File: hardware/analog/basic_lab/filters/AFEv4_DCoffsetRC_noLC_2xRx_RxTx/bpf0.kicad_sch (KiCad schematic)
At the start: 8 parts

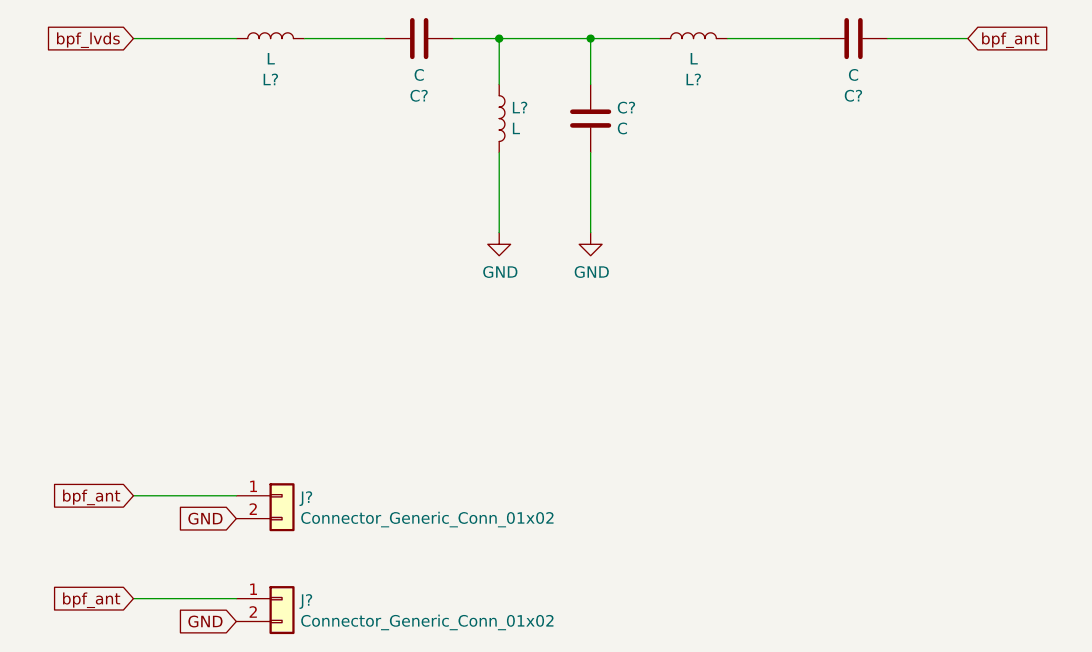
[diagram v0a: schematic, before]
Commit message: started 2xRx / RxTx PCBs with no / simple LC filters
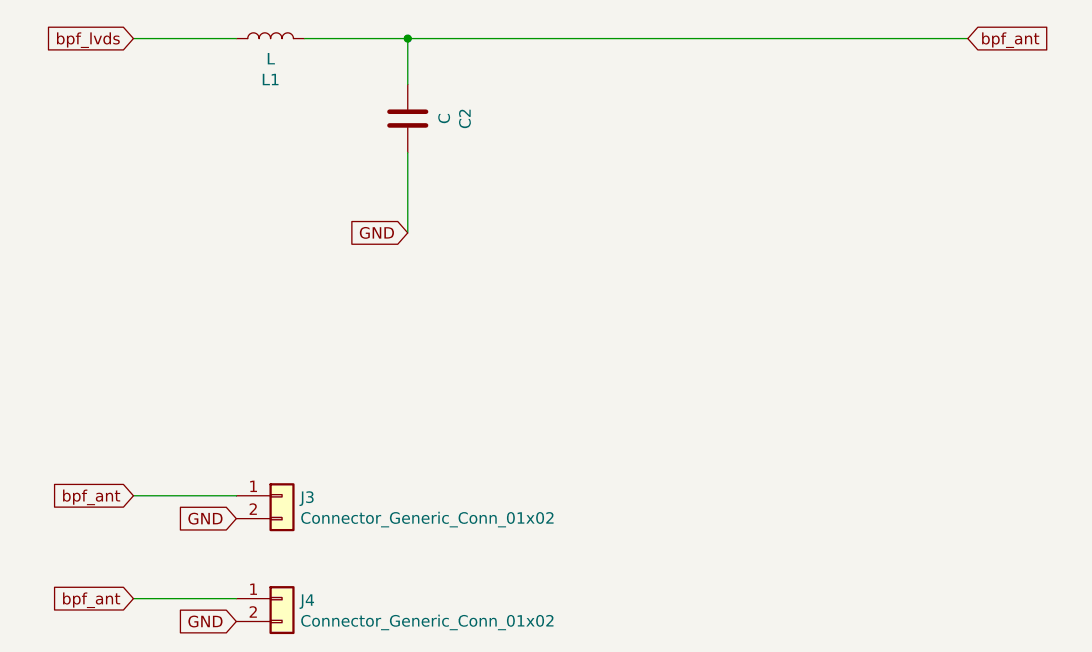
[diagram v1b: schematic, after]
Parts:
- removed C? (x2): C, Capacitor_THT:C_Axial_L3.8mm_D2.6mm_P7.50mm_Horizontal, symbol Device:C
- removed L? (x2): L, Inductor_THT:L_Toroid_Horizontal_D12.7mm_P20.00mm_Diameter14-5mm_Amidon-T50, symbol Device:L
- gave numbers to parts that had none: 4
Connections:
- net GND: now also C2.1
- net bpf_ant: now also C2.2, L1.2
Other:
- moved on the sheet: C2
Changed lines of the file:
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@@
 (kicad_sch (version 20211123) (generator eeschema)
   (paper "A4")
-  (junction (at 105.41 68.58) (diameter 0) (color 0 0 0 0)
-  )
-  (junction (at 95.25 68.58) (diameter 0) (color 0 0 0 0)
-  )
-  (wire (pts (xy 95.25 73.66) (xy 95.25 68.58))
-    (stroke (width 0) (type default) (color 0 0 0 0))
+  (junction (at 85.09 68.58) (diameter 0) (color 0 0 0 0)
   )
   (wire (pts (xy 54.61 119.38) (xy 66.04 119.38))
     (stroke (width 0) (type default) (color 0 0 0 0))
   )
-  (wire (pts (xy 95.25 68.58) (xy 90.17 68.58))
+  (wire (pts (xy 85.09 68.58) (xy 85.09 73.66))
     (stroke (width 0) (type default) (color 0 0 0 0))
   )
-  (wire (pts (xy 147.32 68.58) (xy 138.43 68.58))
+  (wire (pts (xy 73.66 68.58) (xy 85.09 68.58))
     (stroke (width 0) (type default) (color 0 0 0 0))
   )
-  (wire (pts (xy 105.41 90.17) (xy 105.41 81.28))
+  (wire (pts (xy 85.09 68.58) (xy 147.32 68.58))
     (stroke (width 0) (type default) (color 0 0 0 0))
   )
-  (wire (pts (xy 95.25 68.58) (xy 105.41 68.58))
-    (stroke (width 0) (type default) (color 0 0 0 0))
-  )
-  (wire (pts (xy 82.55 68.58) (xy 73.66 68.58))
+  (wire (pts (xy 85.09 81.28) (xy 85.09 90.17))
     (stroke (width 0) (type default) (color 0 0 0 0))
   )
@@
     (stroke (width 0) (type default) (color 0 0 0 0))
   )
-  (wire (pts (xy 130.81 68.58) (xy 120.65 68.58))
-    (stroke (width 0) (type default) (color 0 0 0 0))
-  )
   (wire (pts (xy 66.04 68.58) (xy 54.61 68.58))
-    (stroke (width 0) (type default) (color 0 0 0 0))
-  )
-  (wire (pts (xy 113.03 68.58) (xy 105.41 68.58))
-    (stroke (width 0) (type default) (color 0 0 0 0))
-  )
-  (wire (pts (xy 95.25 81.28) (xy 95.25 90.17))
-    (stroke (width 0) (type default) (color 0 0 0 0))
-  )
-  (wire (pts (xy 105.41 73.66) (xy 105.41 68.58))
     (stroke (width 0) (type default) (color 0 0 0 0))
   )
@@
     )
   )
-  (symbol (lib_id "Device:C") (at 86.36 68.58 90) (unit 1)
-    (in_bom yes) (on_board yes)
-    (property "Reference" "C?" (id 0) (at 86.36 74.9808 90))
-    (property "Value" "C" (id 1) (at 86.36 72.6694 90))
-    (property "Footprint" "Capacitor_THT:C_Axial_L3.8mm_D2.6mm_P7.50mm_Horizontal" (id 2) (at 90.17 67.6148 0)
+  (global_label "GND" (shape input) (at 85.09 90.17 180) (fields_autoplaced)
+    (effects (font (size 1.27 1.27)) (justify right))
+    (property "Intersheet References" "${INTERSHEET_REFS}" (id 0) (at -45.72 31.75 0)
       (effects (font (size 1.27 1.27)) hide)
     )
-    (property "Datasheet" "~" (id 3) (at 86.36 68.58 0)
+  )
+  (symbol (lib_id "Device:C") (at 85.09 77.47 180) (unit 1)
+    (in_bom yes) (on_board yes)
+    (property "Reference" "C2" (id 0) (at 91.4908 77.47 90))
+    (property "Value" "C" (id 1) (at 89.1794 77.47 90))
+    (property "Footprint" "Capacitor_THT:C_Axial_L3.8mm_D2.6mm_P7.50mm_Horizontal" (id 2) (at 84.1248 73.66 0)
+      (effects (font (size 1.27 1.27)) hide)
+    )
+    (property "Datasheet" "~" (id 3) (at 85.09 77.47 0)
       (effects (font (size 1.27 1.27)) hide)
     )
@@
     (pin "2")
   )
-  (symbol (lib_id "power:GND") (at 105.41 90.17 0) (unit 1)
-    (in_bom yes) (on_board yes)
-    (property "Reference" "#PWR?" (id 0) (at 105.41 96.52 0)
-      (effects (font (size 1.27 1.27)) hide)
-    )
-    (property "Value" "GND" (id 1) (at 105.537 94.5642 0))
-    (property "Footprint" "" (id 2) (at 105.41 90.17 0)
-      (effects (font (size 1.27 1.27)) hide)
-    )
-    (property "Datasheet" "" (id 3) (at 105.41 90.17 0)
-      (effects (font (size 1.27 1.27)) hide)
-    )
-    (pin "1")
-  )
   (symbol (lib_id "bgt:Connector_Generic_Conn_01x02") (at 71.12 130.81 0) (unit 1)
     (in_bom yes) (on_board yes)
-    (property "Reference" "J?" (id 0) (at 73.152 131.0132 0)
+    (property "Reference" "J4" (id 0) (at 73.152 131.0132 0)
       (effects (font (size 1.27 1.27)) (justify left))
     )
@@
   (symbol (lib_id "Device:L") (at 69.85 68.58 90) (unit 1)
     (in_bom yes) (on_board yes)
-    (property "Reference" "L?" (id 0) (at 69.85 73.1774 90))
+    (property "Reference" "L1" (id 0) (at 69.85 73.1774 90))
     (property "Value" "L" (id 1) (at 69.85 70.866 90))
     (property "Footprint" "Inductor_THT:L_Toroid_Horizontal_D12.7mm_P20.00mm_Diameter14-5mm_Amidon-T50" (id 2) (at 69.85 68.58 0)
@@
   (symbol (lib_id "bgt:Connector_Generic_Conn_01x02") (at 71.12 119.38 0) (unit 1)
     (in_bom yes) (on_board yes)
-    (property "Reference" "J?" (id 0) (at 73.152 119.5832 0)
+    (property "Reference" "J3" (id 0) (at 73.152 119.5832 0)
       (effects (font (size 1.27 1.27)) (justify left))
     )
@@
       (effects (font (size 1.27 1.27)) hide)
     )
-    (pin "1")
-    (pin "2")
-  )
-  (symbol (lib_id "Device:C") (at 105.41 77.47 0) (unit 1)
-    (in_bom yes) (on_board yes)
-    (property "Reference" "C?" (id 0) (at 108.331 76.3016 0)
-      (effects (font (size 1.27 1.27)) (justify left))
-    )
-    (property "Value" "C" (id 1) (at 108.331 78.613 0)
-      (effects (font (size 1.27 1.27)) (justify left))
-    )
-    (property "Footprint" "Capacitor_THT:C_Axial_L3.8mm_D2.6mm_P7.50mm_Horizontal" (id 2) (at 106.3752 81.28 0)
-      (effects (font (size 1.27 1.27)) hide)
-    )
-    (property "Datasheet" "~" (id 3) (at 105.41 77.47 0)
-      (effects (font (size 1.27 1.27)) hide)
-    )
-    (pin "1")
-    (pin "2")
-  )
-  (symbol (lib_id "power:GND") (at 95.25 90.17 0) (unit 1)
-    (in_bom yes) (on_board yes)
-    (property "Reference" "#PWR?" (id 0) (at 95.25 96.52 0)
-      (effects (font (size 1.27 1.27)) hide)
-    )
-    (property "Value" "GND" (id 1) (at 95.377 94.5642 0))
-    (property "Footprint" "" (id 2) (at 95.25 90.17 0)
-      (effects (font (size 1.27 1.27)) hide)
-    )
-    (property "Datasheet" "" (id 3) (at 95.25 90.17 0)
-      (effects (font (size 1.27 1.27)) hide)
-    )
-    (pin "1")
-  )
-  (symbol (lib_id "Device:L") (at 116.84 68.58 90) (unit 1)
-    (in_bom yes) (on_board yes)
-    (property "Reference" "L?" (id 0) (at 116.84 73.1774 90))
-    (property "Value" "L" (id 1) (at 116.84 70.866 90))
-    (property "Footprint" "Inductor_THT:L_Toroid_Horizontal_D12.7mm_P20.00mm_Diameter14-5mm_Amidon-T50" (id 2) (at 116.84 68.58 0)
-      (effects (font (size 1.27 1.27)) hide)
-    )
-    (property "Datasheet" "~" (id 3) (at 116.84 68.58 0)
-      (effects (font (size 1.27 1.27)) hide)
-    )
-    (pin "1")
-    (pin "2")
-  )
-  (symbol (lib_id "Device:L") (at 95.25 77.47 0) (unit 1)
-    (in_bom yes) (on_board yes)
-    (property "Reference" "L?" (id 0) (at 96.5962 76.3016 0)
-      (effects (font (size 1.27 1.27)) (justify left))
-    )
-    (property "Value" "L" (id 1) (at 96.5962 78.613 0)
-      (effects (font (size 1.27 1.27)) (justify left))
-    )
-    (property "Footprint" "Inductor_THT:L_Toroid_Horizontal_D12.7mm_P20.00mm_Diameter14-5mm_Amidon-T50" (id 2) (at 95.25 77.47 0)
-      (effects (font (size 1.27 1.27)) hide)
-    )
-    (property "Datasheet" "~" (id 3) (at 95.25 77.47 0)
-      (effects (font (size 1.27 1.27)) hide)
-    )
-    (pin "1")
-    (pin "2")
-  )
-  (symbol (lib_id "Device:C") (at 134.62 68.58 90) (unit 1)
-    (in_bom yes) (on_board yes)
-    (property "Reference" "C?" (id 0) (at 134.62 74.9808 90))
-    (property "Value" "C" (id 1) (at 134.62 72.6694 90))
-    (property "Footprint" "Capacitor_THT:C_Axial_L3.8mm_D2.6mm_P7.50mm_Horizontal" (id 2) (at 138.43 67.6148 0)
-      (effects (font (size 1.27 1.27)) hide)
-    )
-    (property "Datasheet" "~" (id 3) (at 134.62 68.58 0)
-      (effects (font (size 1.27 1.27)) hide)
-    )

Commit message: started 2xRx / RxTx PCBs with no / simple LC filters: Gerber with THT board; started SMD board in the same DIR
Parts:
- C2: footprint Capacitor_THT:C_Axial_L3.8mm_D2.6mm_P7.50mm_Horizontal -> Capacitor_SMD:C_1206_3216Metric
- L1: footprint Inductor_THT:L_Toroid_Horizontal_D12.7mm_P20.00mm_Diameter14-5mm_Amidon-T50 -> Inductor_SMD:L_1206_3216Metric
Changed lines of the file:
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@@
     (property "Reference" "C2" (id 0) (at 91.4908 77.47 90))
     (property "Value" "C" (id 1) (at 89.1794 77.47 90))
-    (property "Footprint" "Capacitor_THT:C_Axial_L3.8mm_D2.6mm_P7.50mm_Horizontal" (id 2) (at 84.1248 73.66 0)
+    (property "Footprint" "Capacitor_SMD:C_1206_3216Metric" (id 2) (at 84.1248 73.66 0)
       (effects (font (size 1.27 1.27)) hide)
     )
@@
     (property "Reference" "L1" (id 0) (at 69.85 73.1774 90))
     (property "Value" "L" (id 1) (at 69.85 70.866 90))
-    (property "Footprint" "Inductor_THT:L_Toroid_Horizontal_D12.7mm_P20.00mm_Diameter14-5mm_Amidon-T50" (id 2) (at 69.85 68.58 0)
+    (property "Footprint" "Inductor_SMD:L_1206_3216Metric" (id 2) (at 69.85 68.58 0)
       (effects (font (size 1.27 1.27)) hide)
     )
